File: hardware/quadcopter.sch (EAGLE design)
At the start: 61 parts, among them J1 AVR_SPI_PRG_6NS, J2 HEADER-4POS-2X2-0.1IN-FEMALE-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, J3 HEADER-10POSTH-254X10, J4 HEADER-4POS-0.1IN-FEMALE-SMD-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, Q1 MOSFET-SI2302CDS-T1-E3CT-ND, Q2 MOSFET-SI2302CDS-T1-E3CT-ND, Q3 MOSFET-SI2302CDS-T1-E3CT-ND, Q4 MOSFET-SI2302CDS-T1-E3CT-ND, Q5 MOSFET-SI2302CDS-T1-E3CT-ND, Q6 MOSFET-SI2302CDS-T1-E3CT-ND, SW1 PUSHBUTTON_SMD-VERTICAL-1, U1 ATMEGA128RFA1, U2 LSM-IMU-497-18367-1-NDIMU, Y1 CRYSTAL5X3

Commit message: tried fixing the warnings
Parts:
- removed C13: 1uF, quadparts_prebuilt_2022:CAPACITOR-NP_SMD-0603_CERAMIC-1UF
- removed R12: 10K, custom.lbr:RESISTOR_SMD-0603-10K
- removed R14: 20, custom.lbr:RESISTOR_-20-OHM
- added C15: 4.7uF, quadparts_prebuilt_2022:CAPACITOR-NP_SMD-2012-0805_CERAMIC-4.7UF
- added C16: 1uF, quadparts_prebuilt_2022:CAPACITOR-NP_SMD-2012-0805_CERAMIC-4.7UF
- added R16: 10K, custom.lbr:MY-RESISTOR-08050OHMRES
- added R17: 20, custom.lbr:MY-RESISTOR-08050OHMRES
- R13: device custom.lbr:RESISTOR_-20-OHM -> custom.lbr:MY-RESISTOR-08050OHMRES
- R15: device custom.lbr:RESISTOR_SMD-0603-10K -> custom.lbr:MY-RESISTOR-08050OHMRES
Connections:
- net GND: now also C16.2, R15.2, R16.2; no longer C13.2, R12.1, R15.1
- net N$13: now also R15.1, R17.2; no longer R12.2, R14.1
- net N$19: now also R16.1; no longer R15.2
- net N$21: now also R17.1; no longer R14.2
- net VBAT: now also C16.1; no longer C13.1

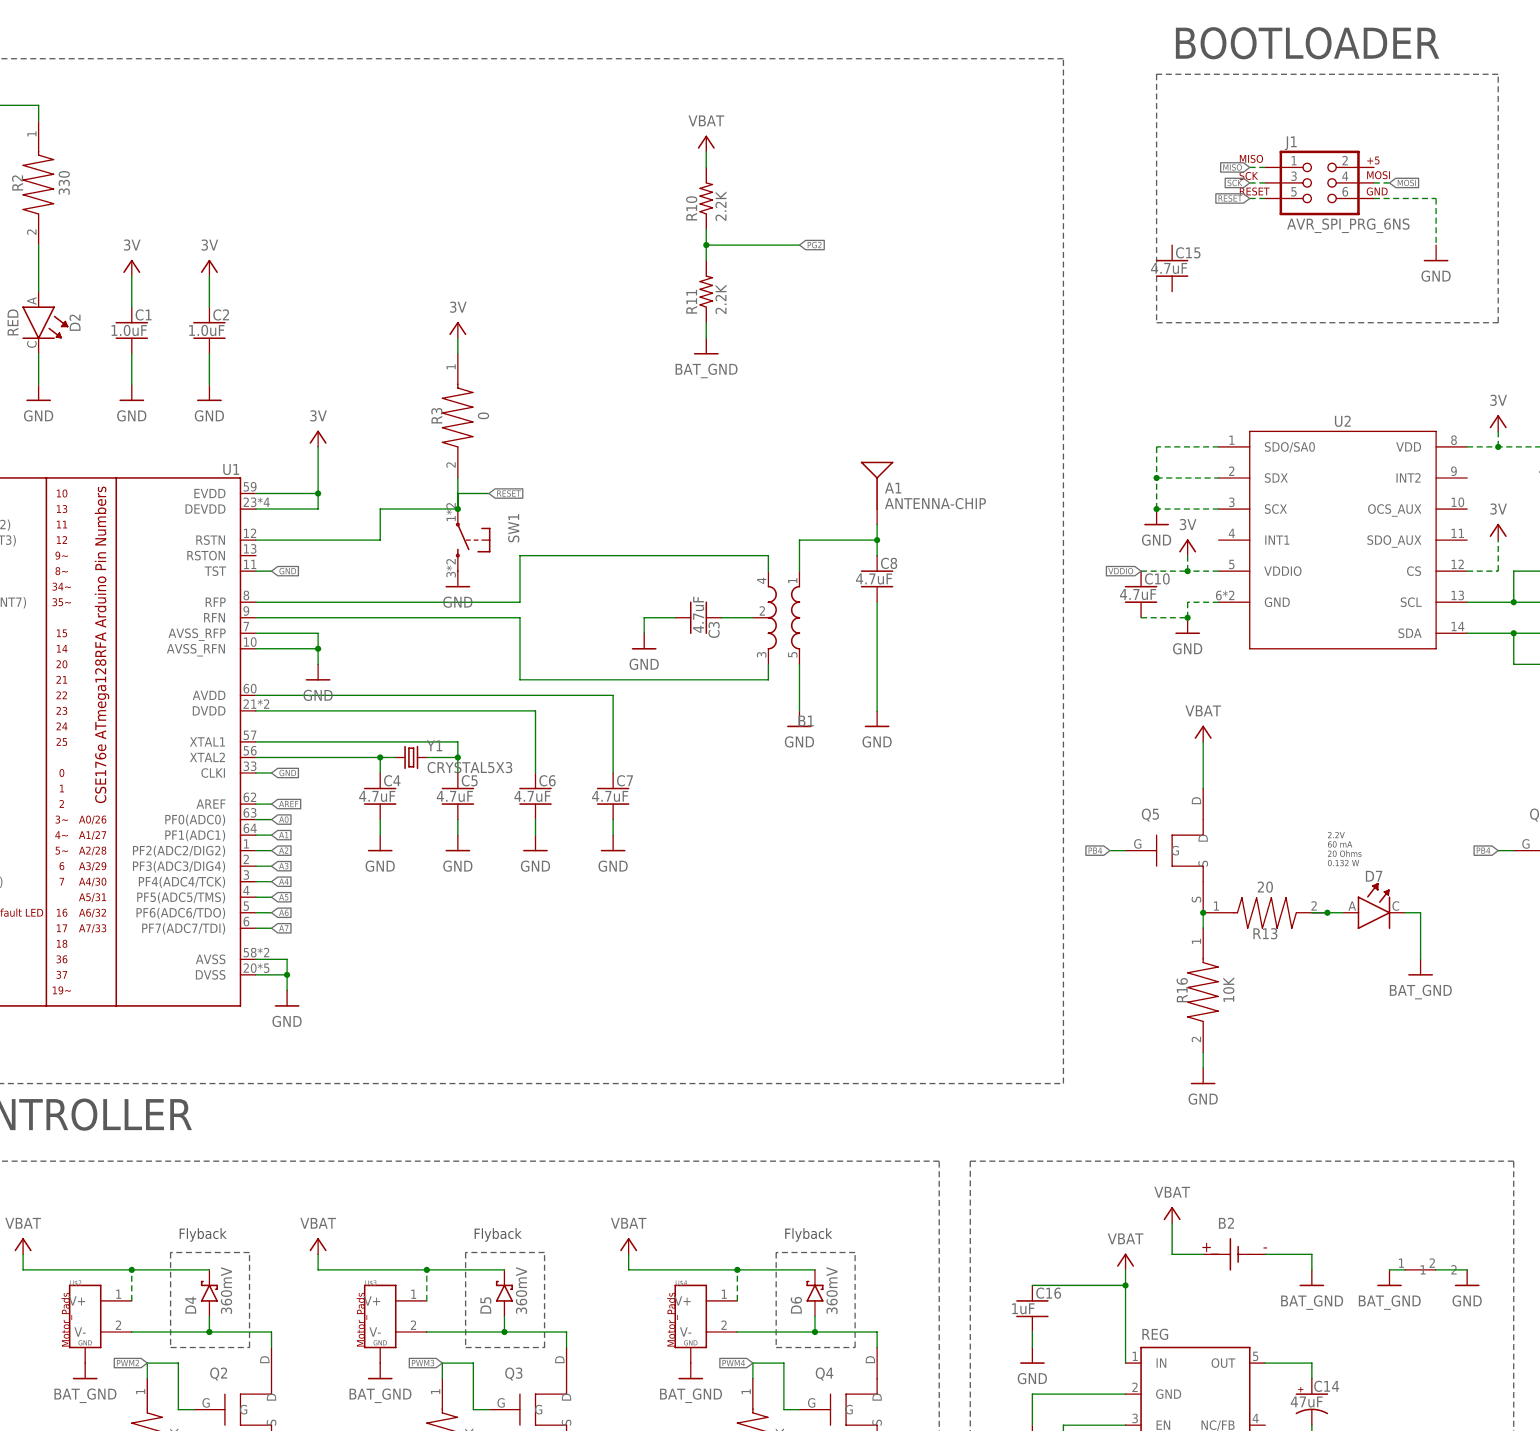
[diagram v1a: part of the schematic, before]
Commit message: updated libraries and renamed custom for submit
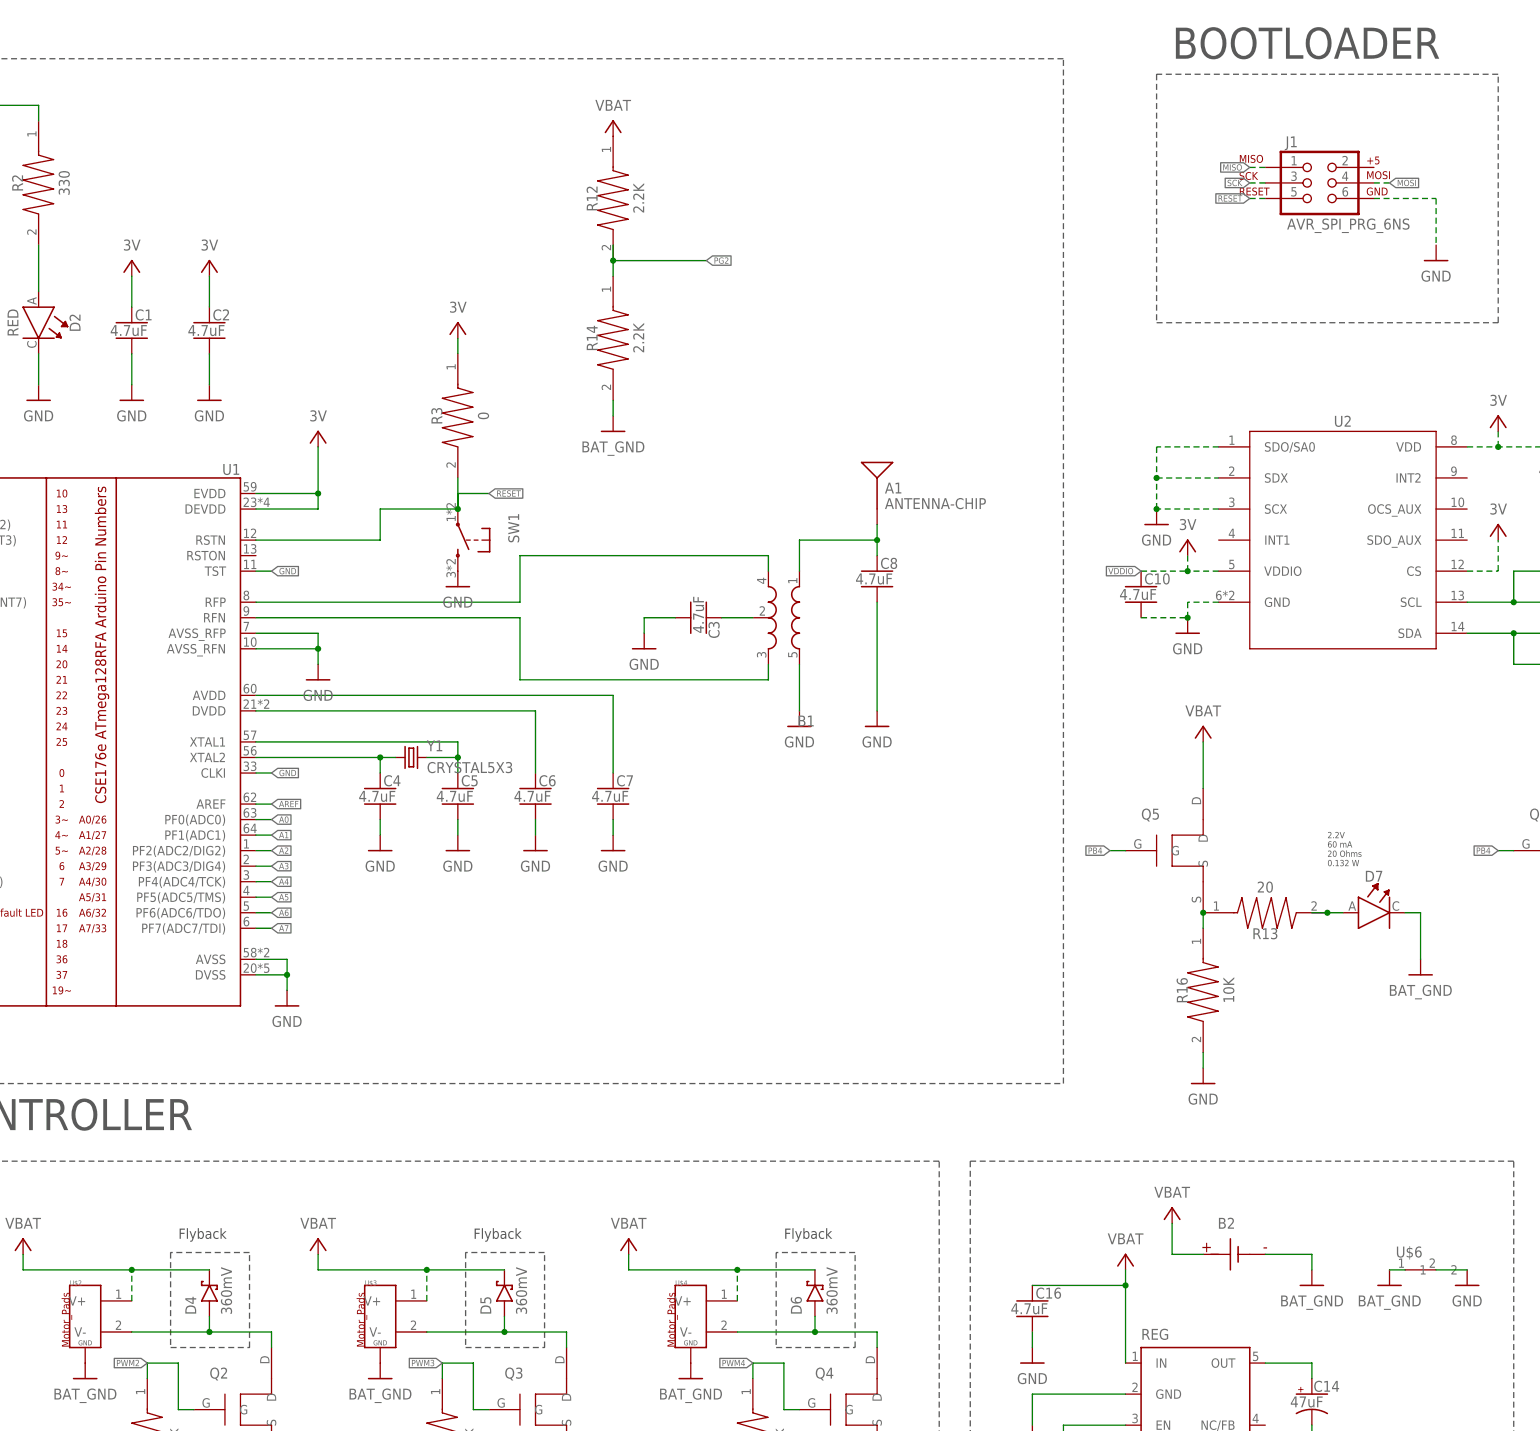
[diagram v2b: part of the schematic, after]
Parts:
- removed C15: 4.7uF, quadparts_prebuilt_2022:CAPACITOR-NP_SMD-2012-0805_CERAMIC-4.7UF
- removed R10, R11: 2.2K, quadparts_prebuilt_2022:RESISTOR_SMD-0603-2.2K
- added R12, R14: 2.2K, custom.lbr:MY-RESISTOR-08050OHMRES
- C1, C2: value 1.0uF -> 4.7uF
- C16: value 1uF -> 4.7uF
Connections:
- net BAT_GND: now also R14.2; no longer R11.1
- net PG2: now also R12.2, R14.1; no longer R10.1, R11.2
- net VBAT: now also R12.1; no longer R10.2

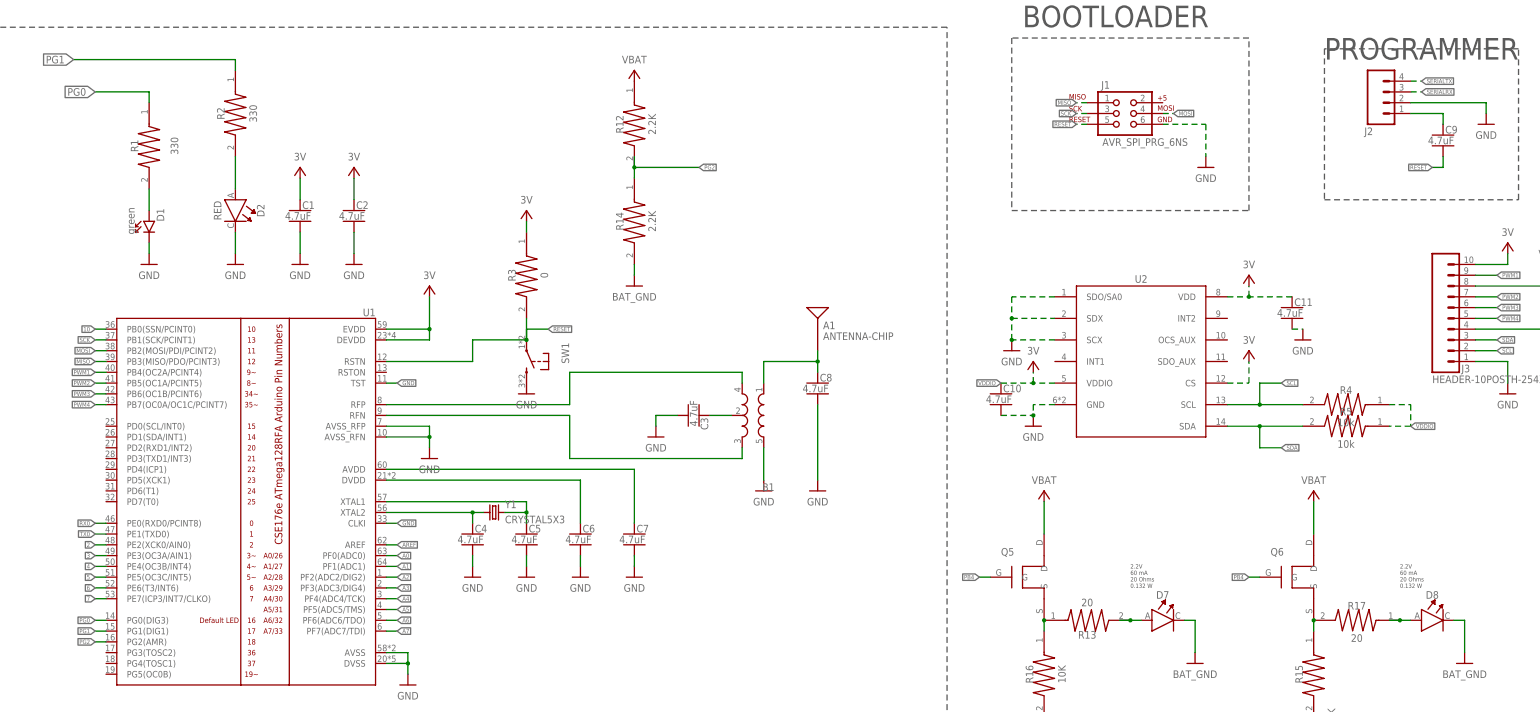
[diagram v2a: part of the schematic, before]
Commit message: removed extra pins
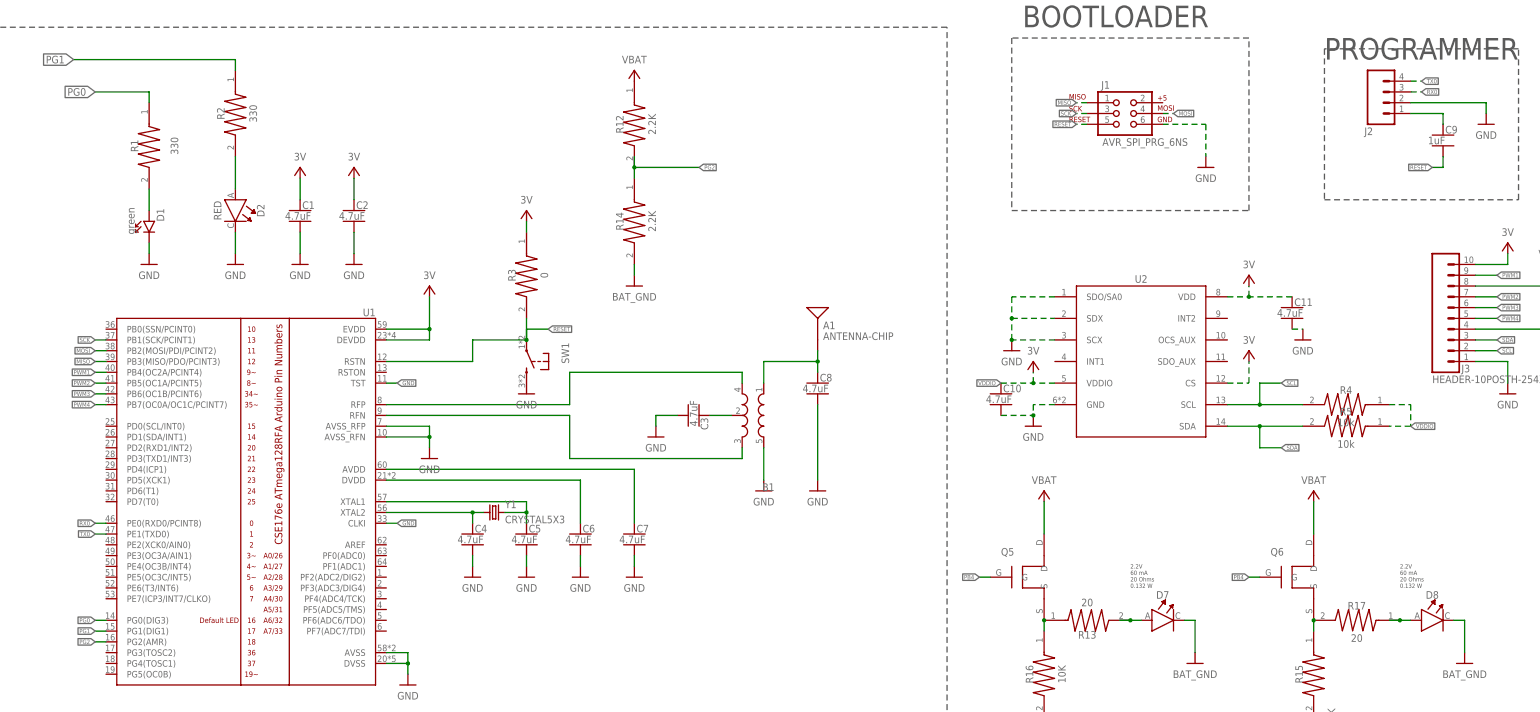
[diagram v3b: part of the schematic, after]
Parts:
- C9: value 4.7uF -> 1uF
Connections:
- removed net 10: U1.PB0(SSN/PCINT0)
- removed net 2: U1.PE2(XCK0/AIN0)
- removed net 3: U1.PE3(OC3A/AIN1)
- removed net 4: U1.PE4(OC3B/INT4)
- removed net 5: U1.PE5(OC3C/INT5)
- removed net 6: U1.PE6(T3/INT6)
- removed net 7: U1.PE7(ICP3/INT7/CLKO)
- removed net A0: U1.PF0(ADC0)
- removed net A1: U1.PF1(ADC1)
- removed net A2: U1.PF2(ADC2/DIG2)
- removed net A3: U1.PF3(ADC3/DIG4)
- removed net A4: U1.PF4(ADC4/TCK)
- removed net A5: U1.PF5(ADC5/TMS)
- removed net A6: U1.PF6(ADC6/TDO)
- removed net A7: U1.PF7(ADC7/TDI)
- removed net AREF: U1.AREF
- removed net SERIALRX: J2.3
- removed net SERIALTX: J2.4
- net RX0: now also J2.3
- net TX0: now also J2.4
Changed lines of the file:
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@@
 <part name="J2" library="quadparts_prebuilt_2022" deviceset="HEADER-4POS" device="-2X2-0.1IN-FEMALE-SMD-BOTTOM-ENTRY"/>
 <part name="GND16" library="quadparts_prebuilt_2022" deviceset="GND" device=""/>
-<part name="C9" library="quadparts_prebuilt_2022" deviceset="CAPACITOR-NP_" device="SMD-2012-0805_CERAMIC-4.7UF" value="4.7uF"/>
+<part name="C9" library="quadparts_prebuilt_2022" deviceset="CAPACITOR-NP_" device="SMD-2012-0805_CERAMIC-4.7UF" value="1uF"/>
 <part name="U2" library="custom.lbr" library_urn="urn:adsk.wipprod:fs.file:vf.FjMADskDQ2Se9fX1PD5xcw" deviceset="LSM-IMU" device="-497-18367-1-NDIMU"/>
 <part name="P+5" library="quadparts_prebuilt_2022" deviceset="3V" device=""/>
@@
 </segment>
 </net>
-<net name="10" class="0">
-<segment>
-<pinref part="U1" gate="G$1" pin="PB0(SSN/PCINT0)"/>
-<wire x1="17.78" y1="165.1" x2="15.24" y2="165.1" width="0.1524" layer="91"/>
-<label x="15.24" y="165.1" size="1.016" layer="95" rot="R180" xref="yes"/>
-</segment>
-</net>
 <net name="SCK" class="0">
 <segment>
@@
 <label x="15.24" y="119.38" size="1.016" layer="95" rot="R180" xref="yes"/>
 </segment>
+<segment>
+<pinref part="J2" gate="G$1" pin="3"/>
+<wire x1="325.12" y1="220.98" x2="327.66" y2="220.98" width="0.1524" layer="91" style="longdash"/>
+<label x="327.66" y="220.98" size="1.016" layer="95" xref="yes"/>
+</segment>
 </net>
 <net name="TX0" class="0">
@@
 <label x="15.24" y="116.84" size="1.016" layer="95" rot="R180" xref="yes"/>
 </segment>
-</net>
-<net name="2" class="0">
-<segment>
-<pinref part="U1" gate="G$1" pin="PE2(XCK0/AIN0)"/>
-<wire x1="17.78" y1="114.3" x2="15.24" y2="114.3" width="0.1524" layer="91"/>
-<label x="15.24" y="114.3" size="1.016" layer="95" rot="R180" xref="yes"/>
-</segment>
-</net>
-<net name="3" class="0">
-<segment>
-<pinref part="U1" gate="G$1" pin="PE3(OC3A/AIN1)"/>
-<wire x1="17.78" y1="111.76" x2="15.24" y2="111.76" width="0.1524" layer="91"/>
-<label x="15.24" y="111.76" size="1.016" layer="95" rot="R180" xref="yes"/>
-</segment>
-</net>
-<net name="4" class="0">
-<segment>
-<pinref part="U1" gate="G$1" pin="PE4(OC3B/INT4)"/>
-<wire x1="17.78" y1="109.22" x2="15.24" y2="109.22" width="0.1524" layer="91"/>
-<label x="15.24" y="109.22" size="1.016" layer="95" rot="R180" xref="yes"/>
-</segment>
-</net>
-<net name="5" class="0">
-<segment>
-<pinref part="U1" gate="G$1" pin="PE5(OC3C/INT5)"/>
-<wire x1="17.78" y1="106.68" x2="15.24" y2="106.68" width="0.1524" layer="91"/>
-<label x="15.24" y="106.68" size="1.016" layer="95" rot="R180" xref="yes"/>
-</segment>
-</net>
-<net name="6" class="0">
-<segment>
-<pinref part="U1" gate="G$1" pin="PE6(T3/INT6)"/>
-<wire x1="17.78" y1="104.14" x2="15.24" y2="104.14" width="0.1524" layer="91"/>
-<label x="15.24" y="104.14" size="1.016" layer="95" rot="R180" xref="yes"/>
-</segment>
-</net>
-<net name="7" class="0">
-<segment>
-<pinref part="U1" gate="G$1" pin="PE7(ICP3/INT7/CLKO)"/>
-<wire x1="17.78" y1="101.6" x2="15.24" y2="101.6" width="0.1524" layer="91"/>
-<label x="15.24" y="101.6" size="1.016" layer="95" rot="R180" xref="yes"/>
+<segment>
+<pinref part="J2" gate="G$1" pin="4"/>
+<wire x1="325.12" y1="223.52" x2="327.66" y2="223.52" width="0.1524" layer="91" style="longdash"/>
+<label x="327.66" y="223.52" size="1.016" layer="95" xref="yes"/>
 </segment>
 </net>
@@
 </segment>
 </net>
-<net name="AREF" class="0">
-<segment>
-<pinref part="U1" gate="G$1" pin="AREF"/>
-<wire x1="83.82" y1="114.3" x2="86.36" y2="114.3" width="0.1524" layer="91"/>
-<label x="86.36" y="114.3" size="1.016" layer="95" xref="yes"/>
-</segment>
-</net>
-<net name="A0" class="0">
-<segment>
-<pinref part="U1" gate="G$1" pin="PF0(ADC0)"/>
-<wire x1="83.82" y1="111.76" x2="86.36" y2="111.76" width="0.1524" layer="91"/>
-<label x="86.36" y="111.76" size="1.016" layer="95" xref="yes"/>
-</segment>
-</net>
-<net name="A1" class="0">
-<segment>
-<pinref part="U1" gate="G$1" pin="PF1(ADC1)"/>
-<wire x1="83.82" y1="109.22" x2="86.36" y2="109.22" width="0.1524" layer="91"/>
-<label x="86.36" y="109.22" size="1.016" layer="95" xref="yes"/>
-</segment>
-</net>
-<net name="A2" class="0">
-<segment>
-<pinref part="U1" gate="G$1" pin="PF2(ADC2/DIG2)"/>
-<wire x1="83.82" y1="106.68" x2="86.36" y2="106.68" width="0.1524" layer="91"/>
-<label x="86.36" y="106.68" size="1.016" layer="95" xref="yes"/>
-</segment>
-</net>
-<net name="A3" class="0">
-<segment>
-<pinref part="U1" gate="G$1" pin="PF3(ADC3/DIG4)"/>
-<wire x1="83.82" y1="104.14" x2="86.36" y2="104.14" width="0.1524" layer="91"/>
-<label x="86.36" y="104.14" size="1.016" layer="95" xref="yes"/>
-</segment>
-</net>
-<net name="A4" class="0">
-<segment>
-<pinref part="U1" gate="G$1" pin="PF4(ADC4/TCK)"/>
-<wire x1="83.82" y1="101.6" x2="86.36" y2="101.6" width="0.1524" layer="91"/>
-<label x="86.36" y="101.6" size="1.016" layer="95" xref="yes"/>
-</segment>
-</net>
-<net name="A5" class="0">
-<segment>
-<pinref part="U1" gate="G$1" pin="PF5(ADC5/TMS)"/>
-<wire x1="83.82" y1="99.06" x2="86.36" y2="99.06" width="0.1524" layer="91"/>
-<label x="86.36" y="99.06" size="1.016" layer="95" xref="yes"/>
-</segment>
-</net>
-<net name="A6" class="0">
-<segment>
-<pinref part="U1" gate="G$1" pin="PF6(ADC6/TDO)"/>
-<wire x1="83.82" y1="96.52" x2="86.36" y2="96.52" width="0.1524" layer="91"/>
-<label x="86.36" y="96.52" size="1.016" layer="95" xref="yes"/>
-</segment>
-</net>
-<net name="A7" class="0">
-<segment>
-<pinref part="U1" gate="G$1" pin="PF7(ADC7/TDI)"/>
-<wire x1="83.82" y1="93.98" x2="86.36" y2="93.98" width="0.1524" layer="91"/>
-<label x="86.36" y="93.98" size="1.016" layer="95" xref="yes"/>
-</segment>
-</net>
 <net name="N$10" class="0">
 <segment>
@@
 </segment>
 </net>
-<net name="SERIALTX" class="0">
-<segment>
-<pinref part="J2" gate="G$1" pin="4"/>
-<wire x1="325.12" y1="223.52" x2="327.66" y2="223.52" width="0.1524" layer="91" style="longdash"/>
-<label x="327.66" y="223.52" size="1.016" layer="95" xref="yes"/>
-</segment>
-</net>
-<net name="SERIALRX" class="0">
-<segment>
-<pinref part="J2" gate="G$1" pin="3"/>
-<wire x1="325.12" y1="220.98" x2="327.66" y2="220.98" width="0.1524" layer="91" style="longdash"/>
-<label x="327.66" y="220.98" size="1.016" layer="95" xref="yes"/>
-</segment>
-</net>
